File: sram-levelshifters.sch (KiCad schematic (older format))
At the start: 15 parts, among them U10 ISSI61WV5128BL, U11 ISSI61WV5128BL, U12 ISSI61WV5128BL, U13 ISSI61WV5128BL, U3 74HC04, U4 TXB0108-PW, U5 TXB0108-PW, U6 TXB0108-PW, U7 74HC04, U8 TXB0108-PW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

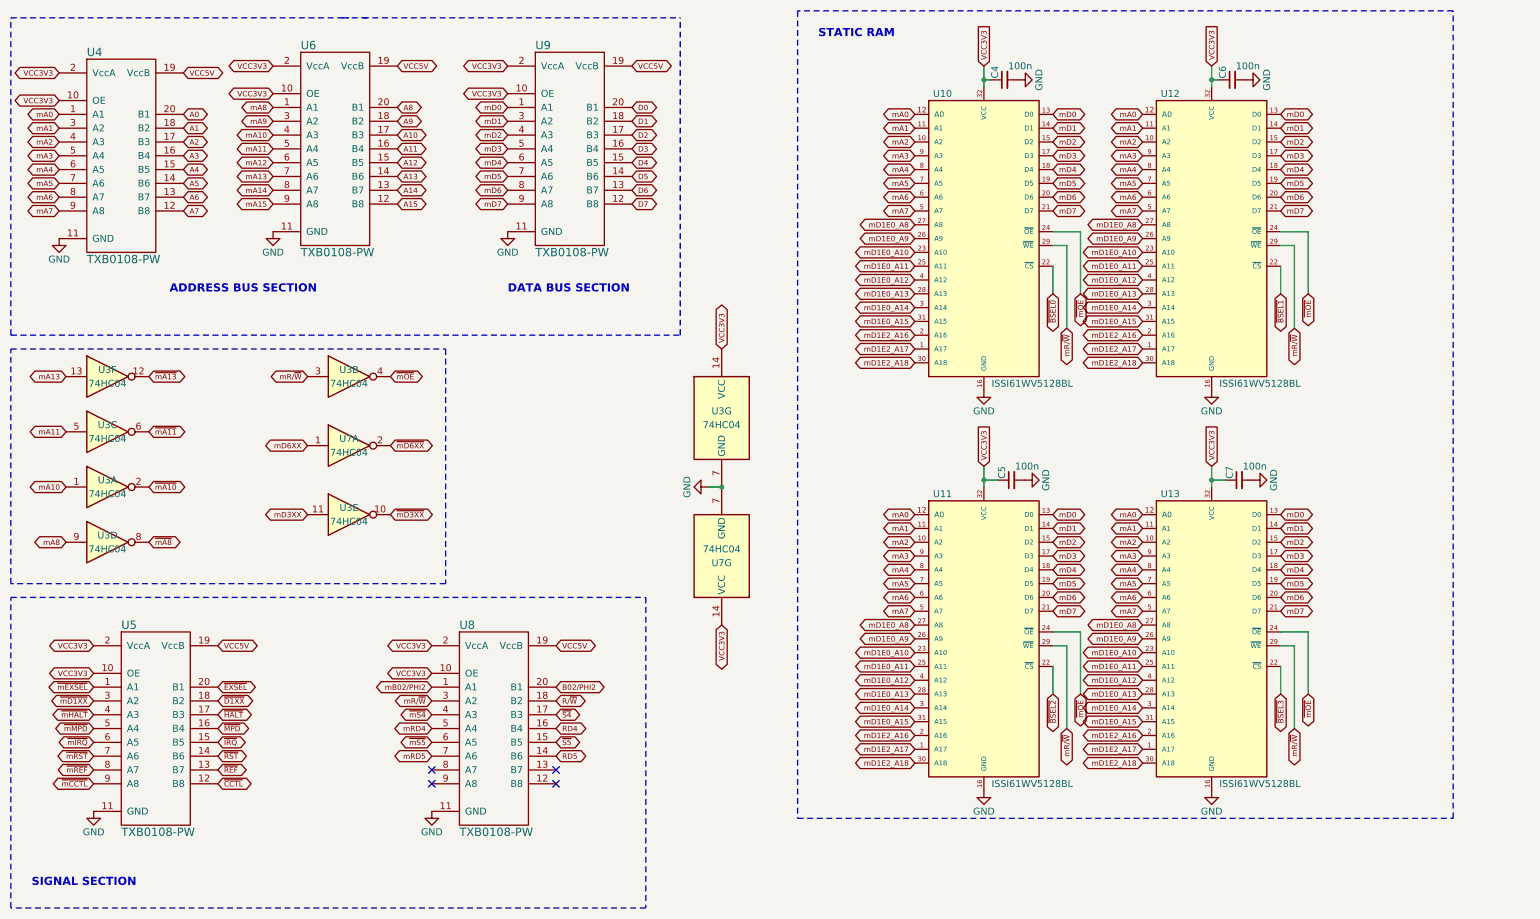
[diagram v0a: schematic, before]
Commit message: Upgraded with the latest infos
Now there is no logic for address/decoding. All is done inside the
microprocessor. This is a semi-final release.
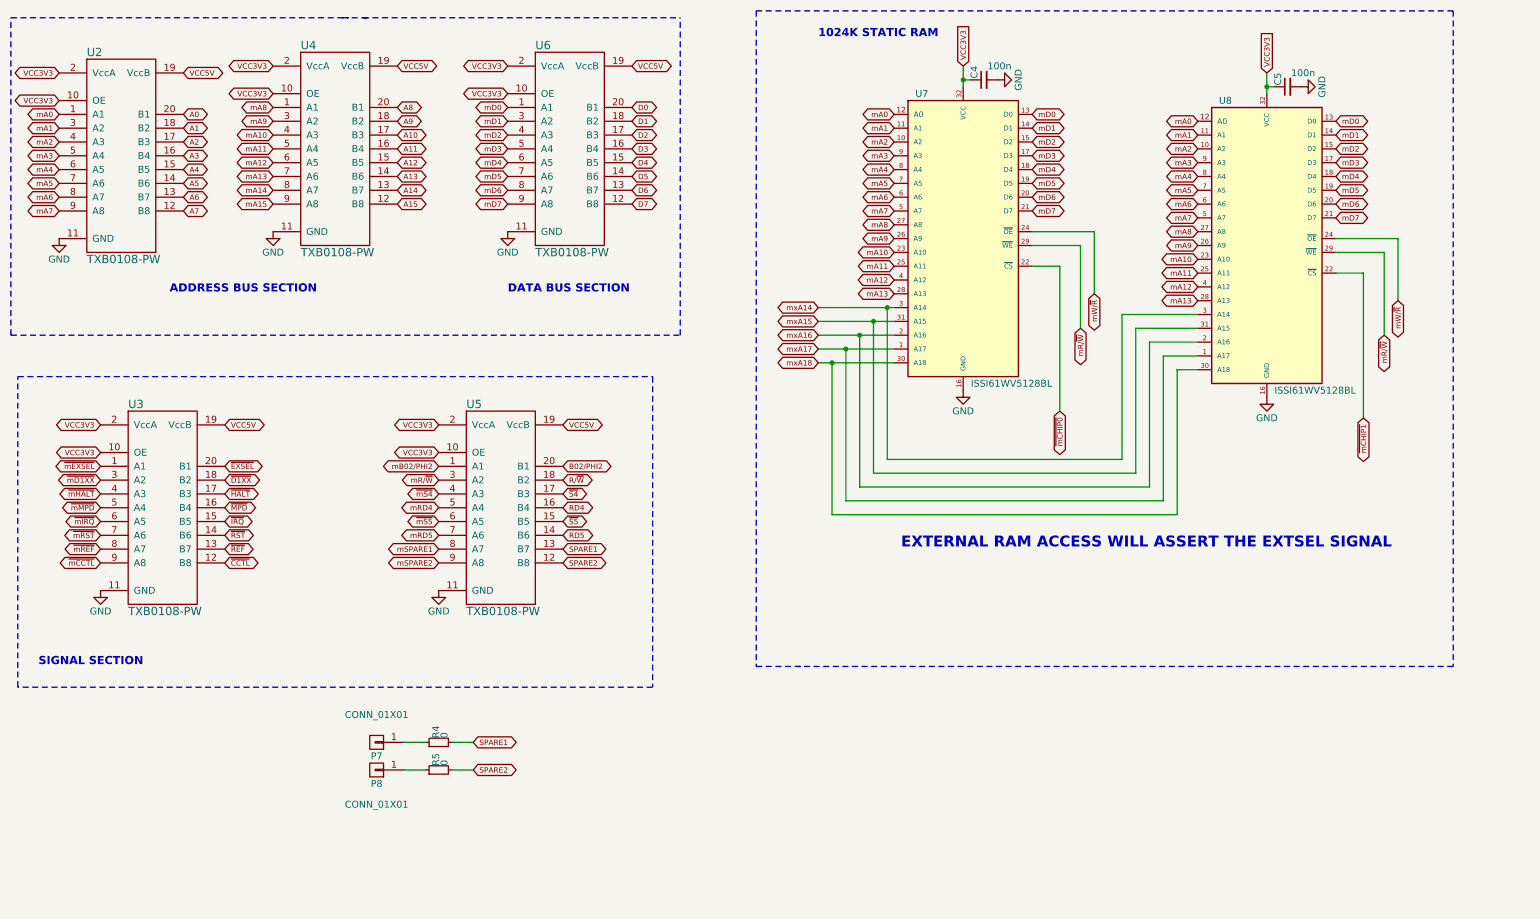
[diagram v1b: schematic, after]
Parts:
- removed C6, C7: 100n, Capacitors_SMD:C_1206_HandSoldering, symbol C_Small
- removed U11, U12, U13: ISSI61WV5128BL, RetroBitLab:SOP-32L-20.5x11.30-1.27mm, symbol ISSI61WV5128BL
- removed U3, U7: 74HC04, Housings_SSOP:TSSOP-14_4.4x5mm_Pitch0.65mm, symbol 74HC04
- added P7, P8: CONN_01X01, TestPoint:TestPoint_Pad_1.5x1.5mm, symbol CONN_01X01
- added R4, R5: 0, Resistors_SMD:R_1206_HandSoldering, symbol R_Small
- added U8: ISSI61WV5128BL, RetroBitLab:SOP-32L-20.5x11.30-1.27mm, symbol ISSI61WV5128BL
- renumbered U4 to U2, U5 to U3, U6 to U4, U8 to U5, U9 to U6, U10 to U7
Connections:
- net mD1E0_A10 is gone; now on net mA10: U7.23 (A10)
- net mD1E0_A11 is gone; now on net mA11: U7.25 (A11)
- net mD1E0_A12 is gone; now on net mA12: U7.4 (A12)
- net mD1E0_A13 is gone; now on net mA13: U7.28 (A13)
- net mD1E0_A8 is gone; now on net mA8: U7.27 (A8)
- net mD1E0_A9 is gone; now on net mA9: U7.26 (A9)
- net GND: now also U8.16 (GND)
- net VCC3V3: now also U8.32 (VCC)
- net mA0: now also U8.12 (A0)
- net mA1: now also U8.11 (A1)
- net mA10: now also U8.23 (A10)
- net mA11: now also U8.25 (A11)
- net mA12: now also U8.4 (A12)
- net mA13: now also U8.28 (A13)
- net mA2: now also U8.10 (A2)
- net mA3: now also U8.9 (A3)
- net mA4: now also U8.8 (A4)
- net mA5: now also U8.7 (A5)
- net mA6: now also U8.6 (A6)
- net mA7: now also U8.5 (A7)
- net mA8: now also U8.27 (A8)
- net mA9: now also U8.26 (A9)
- net mD0: now also U8.13 (D0)
- net mD1: now also U8.14 (D1)
- net mD2: now also U8.15 (D2)
- net mD3: now also U8.17 (D3)
- net mD4: now also U8.18 (D4)
- net mD5: now also U8.19 (D5)
- net mD6: now also U8.20 (D6)
- net mD7: now also U8.21 (D7)
- net mR/~W: now also U8.29 (~WE)
- net SPARE2: now reaches U5.12 (B8)
- net SPARE2: now also R5.2
- net SPARE1: now reaches U5.13 (B7)
- net SPARE1: now also R4.2
- net mSPARE1: now reaches U5.8 (A7)
- net mSPARE2: now reaches U5.9 (A8)
- net mD1E0_A14 renamed mxA14
- net mxA14: now also U8.3 (A14)
- net mD1E0_A15 renamed mxA15
- net mxA15: now also U8.31 (A15)
- net mD1E2_A16 renamed mxA16
- net mxA16: now also U8.2 (A16)
- net mD1E2_A17 renamed mxA17
- net mxA17: now also U8.1 (A17)
- net mD1E2_A18 renamed mxA18
- net mxA18: now also U8.30 (A18)
- net ~BSEL0 renamed ~mCHIP0
- net ~mOE renamed mW/~R
- net mW/~R: now also U8.24 (~OE)
- new net: P7.1 (P1), R4.1
- new net: P8.1 (P1), R5.1
- new net ~mCHIP1: U8.22 (~CS)
- no-connect marks 4 -> 0
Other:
- note added: "1024K STATIC RAM"
- note added: "EXTERNAL RAM ACCESS WILL ASSERT THE EXTSEL SIGNAL"
- note removed: "STATIC RAM"
- moved on the sheet: C4, U3, U5, U7

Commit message: Added comment
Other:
- note added: "EXTERNAL RAM ACCESS WILL ASSERT THE EXTSEL SIGNAL (code)"
- note removed: "EXTERNAL RAM ACCESS WILL ASSERT THE EXTSEL SIGNAL"
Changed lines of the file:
@@
 ~mCHIP0
 Text Notes 7050 4500 0    79   ~ 16
-EXTERNAL RAM ACCESS WILL ASSERT THE EXTSEL SIGNAL
+EXTERNAL RAM ACCESS WILL ASSERT THE EXTSEL SIGNAL (code)
 Text GLabel 3700 4500 0    39   BiDi ~ 0
 mSPARE1

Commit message: Modified for dual processors board
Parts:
- removed P7, P8: CONN_01X01, TestPoint:TestPoint_Pad_1.5x1.5mm, symbol CONN_01X01
- removed R4, R5: 0, Resistors_SMD:R_1206_HandSoldering, symbol R_Small
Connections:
- net SPARE1: no longer names the net of U5.13 (B7)
- net SPARE2: no longer names the net of U5.12 (B8)
- net mSPARE1: no longer names the net of U5.8 (A7)
- net mSPARE2: no longer names the net of U5.9 (A8)
- net mxA14 renamed mB0
- net mxA15 renamed mB1
- net mxA16 renamed mB2
- net mxA17 renamed mB3
- net mxA18 renamed mB4
- net ~mCHIP0 renamed mB5
- net ~mCHIP1 renamed ~mB5
- no-connect marks 0 -> 4

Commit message: C64 Emulation. First run on my beloved ATARI 130XE.
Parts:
- C4, C5: footprint Capacitors_SMD:C_1206_HandSoldering -> Capacitor_SMD:C_1206_3216Metric_Pad1.42x1.75mm_HandSolder; symbol C_Small -> Device1:C_Small
- U2, U3, U4, U5, U6: footprint Housings_SSOP:SSOP-20_4.4x6.5mm_Pitch0.65mm -> Package_SO:SSOP-20_4.4x6.5mm_P0.65mm; symbol TXB0108-PW -> AmigaComponents:TXB0108-PW
- U7, U8: symbol ISSI61WV5128BL -> AmigaComponents:ISSI61WV5128BL

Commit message: RetroBitLab library
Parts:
- U2, U3, U4, U5, U6: symbol AmigaComponents:TXB0108-PW -> RetroBitLab:TXB0108-PW
- U7, U8: symbol AmigaComponents:ISSI61WV5128BL -> RetroBitLab:ISSI61WV5128BL
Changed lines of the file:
@@
 $EndDescr
 $Comp
-L AmigaComponents:ISSI61WV5128BL U7
+L RetroBitLab:ISSI61WV5128BL U7
 U 1 1 5C2B9006
 P 7500 2250
@@
 $EndComp
 $Comp
-L AmigaComponents:TXB0108-PW U2
+L RetroBitLab:TXB0108-PW U2
 U 1 1 5C2BF846
 P 1350 1650
@@
 $EndComp
 $Comp
-L AmigaComponents:TXB0108-PW U3
+L RetroBitLab:TXB0108-PW U3
 U 1 1 5C2BF9CC
 P 1650 4200
@@
 $EndComp
 $Comp
-L AmigaComponents:TXB0108-PW U5
+L RetroBitLab:TXB0108-PW U5
 U 1 1 5C2BFA07
 P 4100 4200
@@
 $EndComp
 $Comp
-L AmigaComponents:TXB0108-PW U6
+L RetroBitLab:TXB0108-PW U6
 U 1 1 5C2BFAD5
 P 4600 1600
@@
 ~mS4
 $Comp
-L AmigaComponents:TXB0108-PW U4
+L RetroBitLab:TXB0108-PW U4
 U 1 1 5C374049
 P 2900 1600
@@
 mW/~R
 $Comp
-L AmigaComponents:ISSI61WV5128BL U8
+L RetroBitLab:ISSI61WV5128BL U8
 U 1 1 5C5E8B61
 P 9700 2300
